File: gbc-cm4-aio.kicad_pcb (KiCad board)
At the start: 4 copper layers, 70.1 x 122.2 mm, 137 parts, among them J1 Conn_01x40, J2 AudioJack2_Ground_Switch, J4 DM3D-SF, J6 Conn_01x11, J7 Conn_01x02, P1 USB_C_Plug_USB2.0, Q1 AO4407C, Q3 2N7002E, SW1 SW_Push, SW2 BOOT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

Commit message: remove global_en, move boot to more accessible location
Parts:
- removed R41: 220R, Resistor_SMD:R_0603_1608Metric
- removed SW5: GLOBAL_EN, Button_Switch_SMD:SW_SPST_B3U-1000P
- moved BOOT 14.5 mm to (195.4, 152.6), turned to 0 degrees
- moved R40 12.6 mm to (192.9, 155.1), turned to 180 degrees
- moved ? 6.06 mm to (202.1, 141.9)
- renumbered SW2 to BOOT
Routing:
- net /GLOBAL_EN: track 77.7 -> 0.00 mm, vias 2 -> 0
- net /RPI_BOOT: track 73.4 -> 63.4 mm
- net Net-(R40-Pad1): track 1.09 -> 2.48 mm
- net Net-(R41-Pad1): track 1.09 -> 0.00 mm
- net GND: vias 479 -> 471
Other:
- board text removed: "Boot"

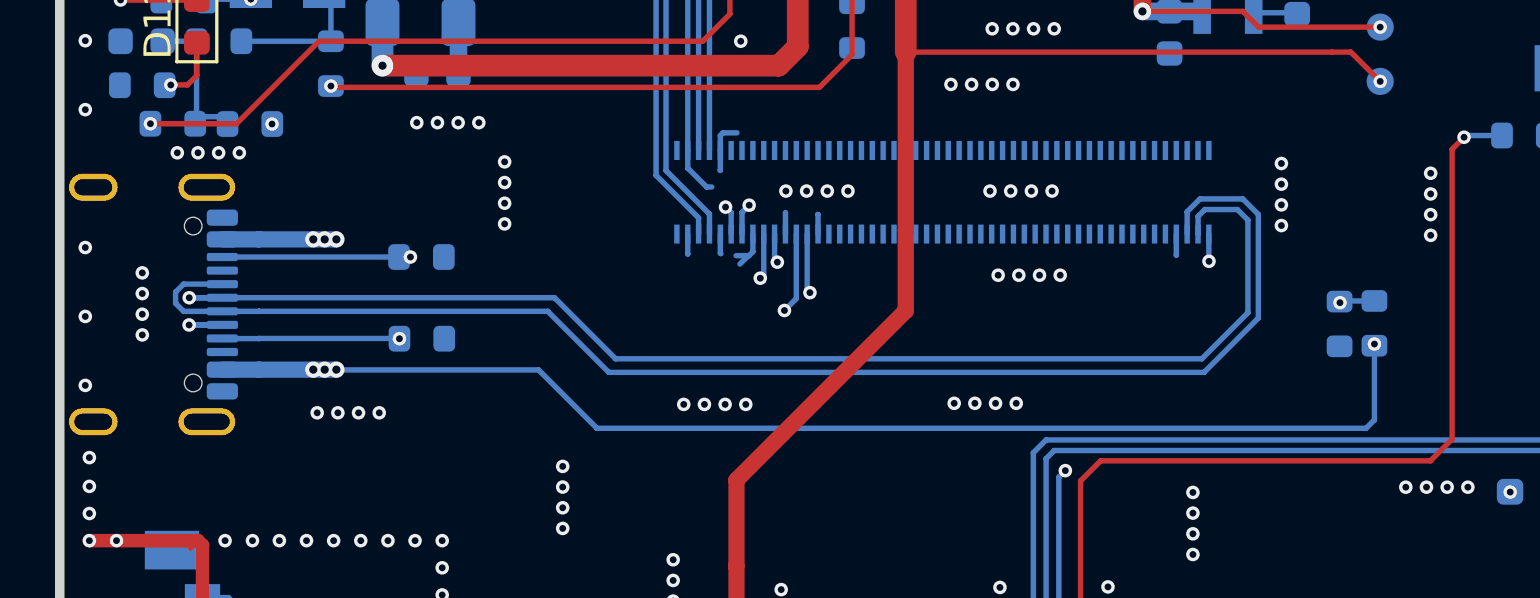
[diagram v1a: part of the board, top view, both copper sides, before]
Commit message: usbc positioning improvement
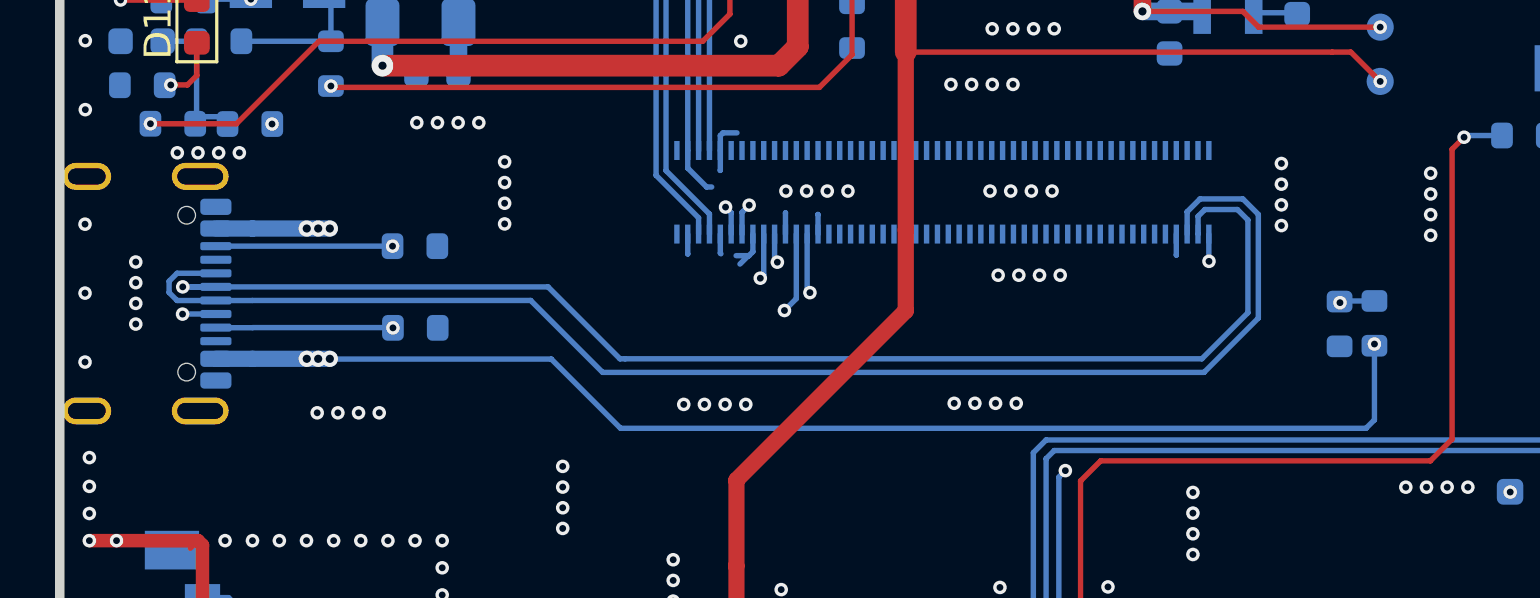
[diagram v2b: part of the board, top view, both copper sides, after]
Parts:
- moved P1 0.47 mm to (141.0, 160.9)
- moved R38 0.47 mm to (152.0, 159.2)
- moved R39 0.47 mm to (152.0, 162.2)
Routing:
- net /IP0: track 37.6 -> 39.6 mm
- net /USB_N: track 51.9 -> 50.9 mm
- net VBUS: track 180.8 -> 181.7 mm

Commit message: volume wheel positioning improvement
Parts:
- moved SW3 0.31 mm to (140.0, 174.8)
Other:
- board text added: "GBC AIO v1.1"
- board text removed: "GBC AIO v1.0"
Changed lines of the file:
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@@
 	(footprint "Button_Switch_SMD:SLLB510100"
 		(layer "B.Cu")
-		(at 140.043 175.1 -90)
+		(at 139.975 174.795 -90)
 		(property "Reference" "SW3"
 			(at 0 -0.175 79)
@@
 		)
 	)
-	(gr_text "GBC AIO v1.0"
+	(gr_text "GBC AIO v1.1"
 		(at 203.664 145.612 0)
 		(layer "B.SilkS")
@@
 	)
 	(segment
-		(start 144 170)
-		(end 140 170)
+		(start 144.1 173.795)
+		(end 144.1 170.1)
 		(width 0.5)
 		(layer "F.Cu")
@@
 	)
 	(segment
-		(start 144.168 170.168)
-		(end 144 170)
+		(start 144 170)
+		(end 140 170)
 		(width 0.5)
 		(layer "F.Cu")
@@
 	)
 	(segment
-		(start 144.168 174.1)
-		(end 144.168 170.168)
+		(start 144.1 170.1)
+		(end 144 170)
 		(width 0.5)
 		(layer "F.Cu")
@@
 	)
 	(via
-		(at 144.168 174.1)
+		(at 144.1 173.795)
 		(size 0.5)
 		(drill 0.25)
@@
 	)
 	(segment
-		(start 145.13 172.1)
-		(end 143.7 172.1)
+		(start 172.847 178.337)
+		(end 171.48 176.97)
 		(width 0.2)
 		(layer "B.Cu")
@@
 	)
 	(segment
-		(start 145.61 177.05)
-		(end 145.61 172.58)
+		(start 145.79 176.65)
+		(end 145.79 172.3)
 		(width 0.2)
 		(layer "B.Cu")
@@
 	)
 	(segment
-		(start 145.61 172.58)
-		(end 145.13 172.1)
+		(start 144.005 171.795)
+		(end 143.7 172.1)
 		(width 0.2)
 		(layer "B.Cu")
@@
 	)
 	(segment
-		(start 172.847 178.447)
-		(end 171.7 177.3)
+		(start 146.11 176.97)
+		(end 145.79 176.65)
 		(width 0.2)
 		(layer "B.Cu")
@@
 	)
 	(segment
-		(start 171.7 177.3)
-		(end 145.86 177.3)
+		(start 172.847 189.544489)
+		(end 172.847 178.337)
 		(width 0.2)
 		(layer "B.Cu")
@@
 	)
 	(segment
-		(start 145.86 177.3)
-		(end 145.61 177.05)
+		(start 171.48 176.97)
+		(end 146.11 176.97)
 		(width 0.2)
 		(layer "B.Cu")
@@
 	)
 	(segment
-		(start 172.847 189.544489)
-		(end 172.847 178.447)
+		(start 145.79 172.3)
+		(end 145.285 171.795)
 		(width 0.2)
 		(layer "B.Cu")
@@
 	)
 	(segment
-		(start 171.562448 177.7)
-		(end 145.41 177.7)
+		(start 145.285 171.795)
+		(end 144.005 171.795)
 		(width 0.2)
 		(layer "B.Cu")
-		(net 196)
+		(net 195)
 	)
 	(segment
-		(start 145.41 177.7)
-		(end 145.16 177.45)
+		(start 145.36 176.87)
+		(end 145.36 176.21)
 		(width 0.2)
 		(layer "B.Cu")
@@
 	)
 	(segment
-		(start 145.16 176.39)
-		(end 144.87 176.1)
+		(start 144.005 175.795)
+		(end 143.7 176.1)
 		(width 0.2)
 		(layer "B.Cu")
@@
 	)
 	(segment
-		(start 145.16 177.45)
-		(end 145.16 176.39)
+		(start 172.447 189.544489)
+		(end 172.447 178.584552)
 		(width 0.2)
 		(layer "B.Cu")
@@
 	)
 	(segment
-		(start 144.87 176.1)
-		(end 143.7 176.1)
+		(start 171.242448 177.38)
+		(end 145.87 177.38)
 		(width 0.2)
 		(layer "B.Cu")
@@
 	(segment
 		(start 172.447 178.584552)
-		(end 171.562448 177.7)
+		(end 171.242448 177.38)
 		(width 0.2)
 		(layer "B.Cu")
@@
 	)
 	(segment
-		(start 172.447 189.544489)
-		(end 172.447 178.584552)
+		(start 145.87 177.38)
+		(end 145.36 176.87)
 		(width 0.2)
 		(layer "B.Cu")
@@
 	)
 	(segment
-		(start 143.7 178.1)
-		(end 171.5 178.1)
+		(start 145.36 176.21)
+		(end 144.945 175.795)
 		(width 0.2)
 		(layer "B.Cu")
-		(net 197)
+		(net 196)
 	)
 	(segment
-		(start 172.047 178.647)
+		(start 144.945 175.795)
+		(end 144.005 175.795)
+		(width 0.2)
+		(layer "B.Cu")
+		(net 196)
+	)
+	(segment
+		(start 172.047 178.767)
 		(end 172.047 189.544489)
 		(width 0.2)
@@
 	)
 	(segment
-		(start 171.5 178.1)
-		(end 172.047 178.647)
+		(start 144.005 177.795)
+		(end 171.075 177.795)
+		(width 0.2)
+		(layer "B.Cu")
+		(net 197)
+	)
+	(segment
+		(start 143.7 178.1)
+		(end 144.005 177.795)
+		(width 0.2)
+		(layer "B.Cu")
+		(net 197)
+	)
+	(segment
+		(start 171.075 177.795)
+		(end 172.047 178.767)
 		(width 0.2)
 		(layer "B.Cu")

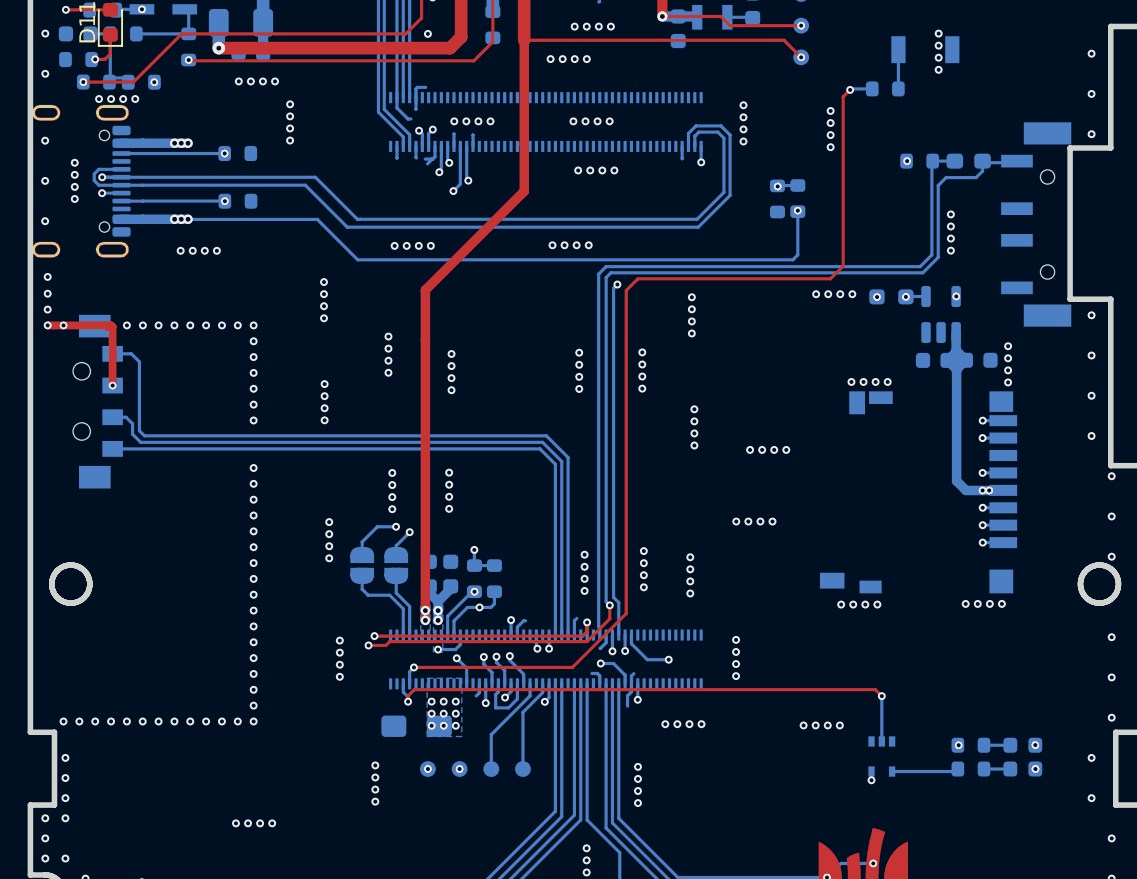
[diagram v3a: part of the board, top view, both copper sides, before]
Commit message: led positioning improvement
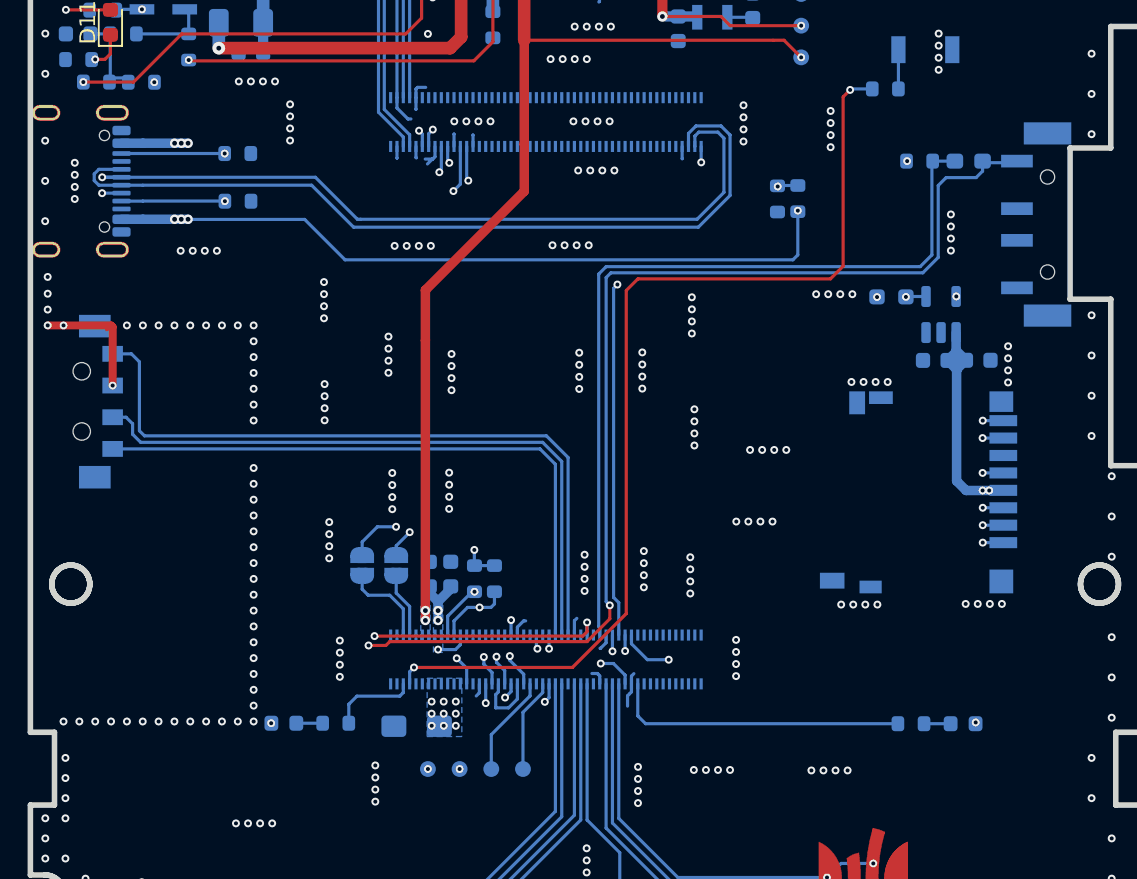
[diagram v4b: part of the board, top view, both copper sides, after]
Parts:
- removed U2: 74LVC1G07SE-7, Package_TO_SOT_SMD:SOT-353_SC-70-5
- D5: value APA2107SECK -> PWR
- D6: value APA2107SECK -> ACT
- moved D5 46.7 mm to (154.9, 195.1), turned to 180 degrees
- moved R7 40.2 mm to (158.2, 195.1), turned to 0 degrees
- moved R8 4.02 mm to (194.5, 195.1)
- moved D6 4.01 mm to (197.8, 195.1)
- renumbered BOOT to SW2
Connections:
- R7 pad 2: Net-(R7-Pad2) -> /PWR_LED
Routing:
- net /PWR_LED: track 34.7 -> 5.72 mm, vias 2 -> 0
- net /ACT_LED: track 23.8 -> 18.7 mm, vias 2 -> 0
- net Net-(R7-Pad2): track 4.22 -> 0.00 mm
- net /+3.3v: track 0.55 -> 0.00 mm, vias 1 -> 0
- net GND: vias 471 -> 467
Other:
- board text added: "ACT"
- board text added: "BOOT"
- board text added: "PWR"
